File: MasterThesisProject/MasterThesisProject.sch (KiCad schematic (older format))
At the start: 25 parts

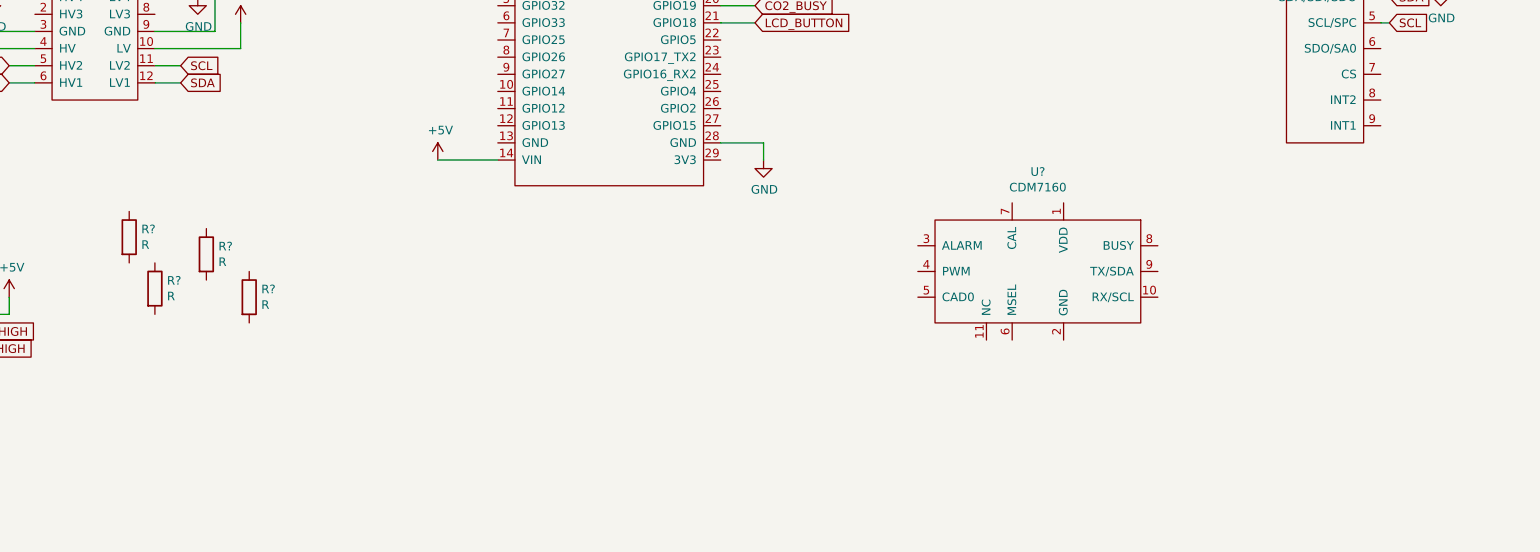
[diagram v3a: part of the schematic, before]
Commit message: Add connections to CDM7160, finish SDA/SCL lines
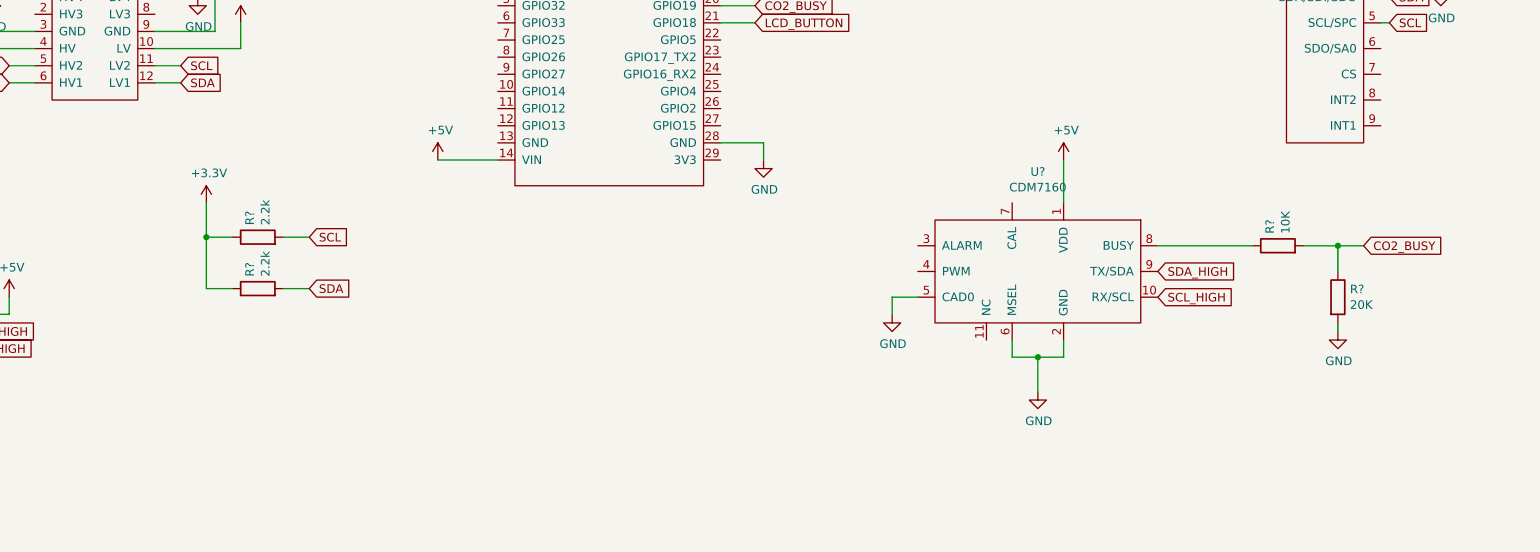
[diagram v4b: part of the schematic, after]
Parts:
- R? (x2): value R -> 2.2k
- R?: value R -> 10K
- R?: value R -> 20K
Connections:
- net +3V3: now also R?.1, R?.1
- net +5V: now also U?.1 (VDD)
- net CO2_BUSY: now also R?.1, R?.2
- net GND: now also R?.2, U?.2 (GND), U?.5 (CAD0), U?.6 (MSEL)
- net SCL: now also R?.2
- net SCL_HIGH: now also U?.10 (RX/SCL)
- net SDA: now also R?.2
- net SDA_HIGH: now also U?.9 (TX/SDA)
- net at R?.1: now also U?.8 (BUSY)
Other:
- moved on the sheet: R?
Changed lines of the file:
@@
 L Device:R R?
 U 1 1 605228A4
-P 2550 5150
-F 0 "R?" H 2620 5196 50  0000 L CNN
-F 1 "R" H 2620 5105 50  0000 L CNN
-F 2 "" V 2480 5150 50  0001 C CNN
-F 3 "~" H 2550 5150 50  0001 C CNN
-	1    2550 5150
-	1    0    0    -1
+P 3300 5150
+F 0 "R?" H 3370 5196 50  0000 L CNN
+F 1 "2.2k" H 3370 5105 50  0000 L CNN
+F 2 "" V 3230 5150 50  0001 C CNN
+F 3 "~" H 3300 5150 50  0001 C CNN
+	1    3300 5150
+	0    -1   -1   0
 $EndComp
 $Comp
 L Device:R R?
 U 1 1 60523294
-P 2700 5450
-F 0 "R?" H 2770 5496 50  0000 L CNN
-F 1 "R" H 2770 5405 50  0000 L CNN
-F 2 "" V 2630 5450 50  0001 C CNN
-F 3 "~" H 2700 5450 50  0001 C CNN
-	1    2700 5450
-	1    0    0    -1
+P 3300 5450
+F 0 "R?" H 3370 5496 50  0000 L CNN
+F 1 "2.2k" H 3370 5405 50  0000 L CNN
+F 2 "" V 3230 5450 50  0001 C CNN
+F 3 "~" H 3300 5450 50  0001 C CNN
+	1    3300 5450
+	0    -1   -1   0
 $EndComp
 $Comp
@@
 L Device:R R?
 U 1 1 605997BB
-P 3000 5250
-F 0 "R?" H 3070 5296 50  0000 L CNN
-F 1 "R" H 3070 5205 50  0000 L CNN
-F 2 "" V 2930 5250 50  0001 C CNN
-F 3 "~" H 3000 5250 50  0001 C CNN
-	1    3000 5250
-	1    0    0    -1
+P 9250 5200
+F 0 "R?" H 9320 5246 50  0000 L CNN
+F 1 "10K" H 9320 5155 50  0000 L CNN
+F 2 "" V 9180 5200 50  0001 C CNN
+F 3 "~" H 9250 5200 50  0001 C CNN
+	1    9250 5200
+	0    -1   -1   0
 $EndComp
 $Comp
 L Device:R R?
 U 1 1 6059A344
-P 3250 5500
-F 0 "R?" H 3320 5546 50  0000 L CNN
-F 1 "R" H 3320 5455 50  0000 L CNN
-F 2 "" V 3180 5500 50  0001 C CNN
-F 3 "~" H 3250 5500 50  0001 C CNN
-	1    3250 5500
+P 9600 5500
+F 0 "R?" H 9670 5546 50  0000 L CNN
+F 1 "20K" H 9670 5455 50  0000 L CNN
+F 2 "" V 9530 5500 50  0001 C CNN
+F 3 "~" H 9600 5500 50  0001 C CNN
+	1    9600 5500
 	1    0    0    -1
 $EndComp
@@
 	1    0    0    -1
 $EndComp
+Text GLabel 8550 5350 2    50   Input ~ 0
+SDA_HIGH
+Text GLabel 8550 5500 2    50   Input ~ 0
+SCL_HIGH
+Wire Wire Line
+	8550 5200 9100 5200
+Wire Wire Line
+	9400 5200 9600 5200
+Wire Wire Line
+	9600 5200 9600 5350
+Wire Wire Line
+	9600 5650 9600 5700
+Wire Wire Line
+	9600 5200 9750 5200
+Connection ~ 9600 5200
+Text GLabel 9750 5200 2    50   Input ~ 0
+CO2_BUSY
+$Comp
+L power:GND #PWR?
+U 1 1 60574544
+P 9600 5700
+F 0 "#PWR?" H 9600 5450 50  0001 C CNN
+F 1 "GND" H 9605 5527 50  0000 C CNN
+F 2 "" H 9600 5700 50  0001 C CNN
+F 3 "" H 9600 5700 50  0001 C CNN
+	1    9600 5700
+	1    0    0    -1
+$EndComp
+Wire Wire Line
+	7150 5500 7000 5500
+Wire Wire Line
+	7000 5500 7000 5600
+Wire Wire Line
+	7850 5850 7850 6050
+$Comp
+L power:GND #PWR?
+U 1 1 6057CB22
+P 7000 5600
+F 0 "#PWR?" H 7000 5350 50  0001 C CNN
+F 1 "GND" H 7005 5427 50  0000 C CNN
+F 2 "" H 7000 5600 50  0001 C CNN
+F 3 "" H 7000 5600 50  0001 C CNN
+	1    7000 5600
+	1    0    0    -1
+$EndComp
+$Comp
+L power:GND #PWR?
+U 1 1 6057D600
+P 7850 6050
+F 0 "#PWR?" H 7850 5800 50  0001 C CNN
+F 1 "GND" H 7855 5877 50  0000 C CNN
+F 2 "" H 7850 6050 50  0001 C CNN
+F 3 "" H 7850 6050 50  0001 C CNN
+	1    7850 6050
+	1    0    0    -1
+$EndComp
+$Comp
+L power:+5V #PWR?
+U 1 1 6057E267
+P 8000 4700
+F 0 "#PWR?" H 8000 4550 50  0001 C CNN
+F 1 "+5V" H 8015 4873 50  0000 C CNN
+F 2 "" H 8000 4700 50  0001 C CNN
+F 3 "" H 8000 4700 50  0001 C CNN
+	1    8000 4700
+	1    0    0    -1
+$EndComp
+Wire Wire Line
+	8000 4700 8000 4950
+Wire Wire Line
+	7700 5750 7700 5850
+Wire Wire Line
+	7700 5850 7850 5850
+Wire Wire Line
+	8000 5850 8000 5750
+Wire Wire Line
+	8000 5850 7850 5850
+Connection ~ 7850 5850
+Wire Wire Line
+	3000 4950 3000 5150
+$Comp
+L power:+3.3V #PWR?
+U 1 1 605946EC
+P 3000 4950
+F 0 "#PWR?" H 3000 4800 50  0001 C CNN
+F 1 "+3.3V" H 3015 5123 50  0000 C CNN
+F 2 "" H 3000 4950 50  0001 C CNN
+F 3 "" H 3000 4950 50  0001 C CNN
+	1    3000 4950
+	1    0    0    -1
+$EndComp
+Wire Wire Line
+	3000 5150 3150 5150
+Connection ~ 3000 5150
+Wire Wire Line
+	3000 5150 3000 5450
+Wire Wire Line
+	3150 5450 3000 5450
+Wire Wire Line
+	3450 5150 3600 5150
+Wire Wire Line
+	3450 5450 3600 5450
+Text GLabel 3600 5150 2    50   Input ~ 0
+SCL
+Text GLabel 3600 5450 2    50   Input ~ 0
+SDA
 $EndSCHEMATC

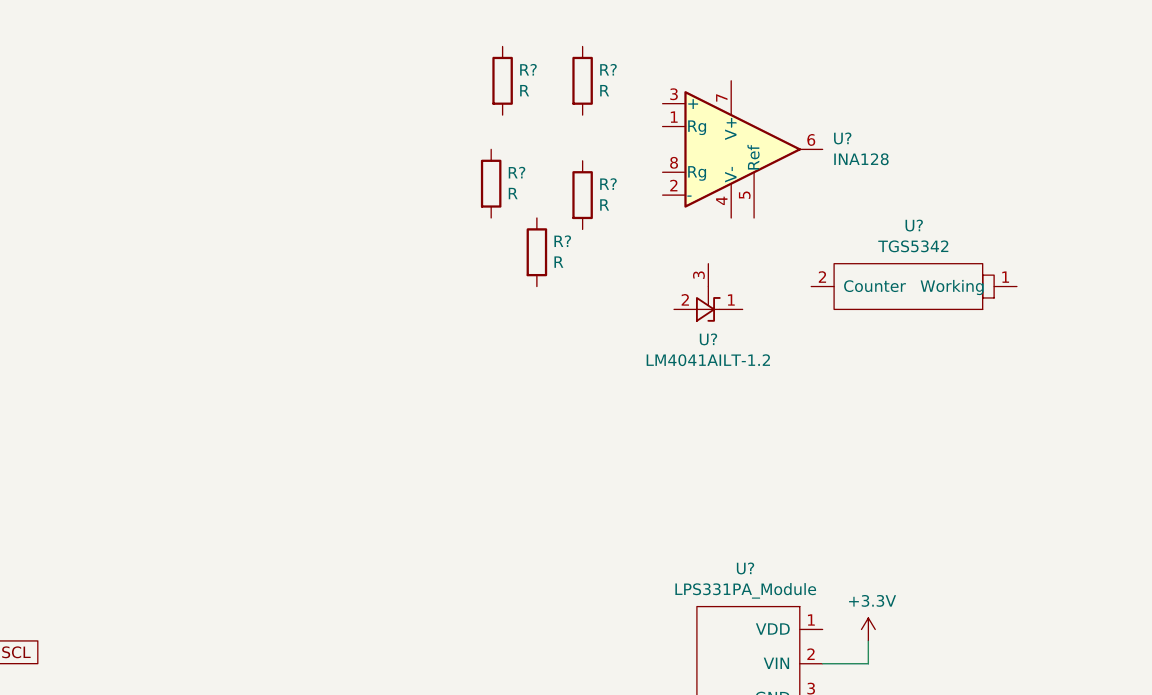
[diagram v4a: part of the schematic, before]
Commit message: Add Carbon Monoxide sensor connections
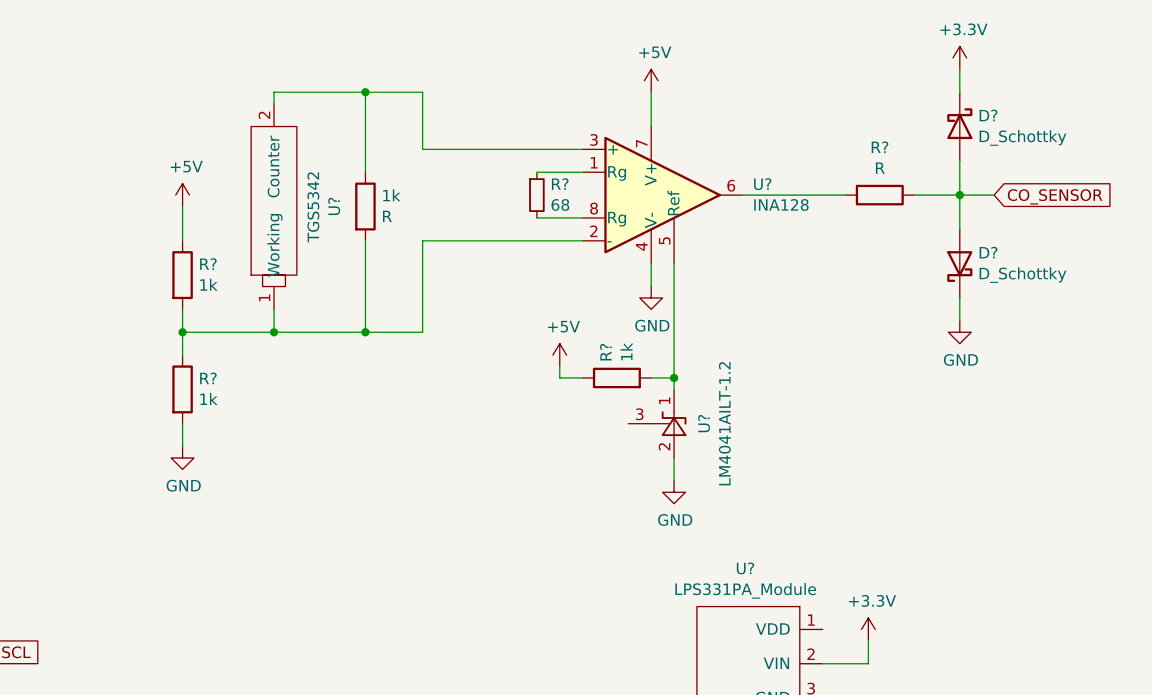
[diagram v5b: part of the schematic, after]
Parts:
- removed R?: R, symbol Device:R
- added D? (x2): D_Schottky, symbol Device:D_Schottky
- added R?: 68, symbol Device:R_Small
- added R?: R, symbol Device:R
- R? (x3): value R -> 1k
- gave numbers to parts that had none: 1
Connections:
- net +3V3: now also D?.1 (K)
- net +5V: now also R?.1, R?.1, U?.7 (V+)
- net GND: now also R?.2, U?.2 (A), U?.4 (V-), D?.1 (K)
- net at R?.2: now also 1k.2, R?.1, U?.1 (Working), U?.2 (-)
- net at 1k.1: now also U?.2 (Counter), U?.3 (+)
- net at U?.1 (Rg): now also R?.1
- net at U?.5 (Ref): now also R?.2, U?.1 (K)
- net at U?.6: now also R?.2
- net at U?.8 (Rg): now also R?.2
- new net CO_SENSOR: D?.2 (A), D?.2 (A), R?.1
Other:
- moved on the sheet: 1k, R?, U?
